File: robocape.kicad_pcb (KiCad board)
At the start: 4 copper layers, 86.4 x 54.6 mm, 110 parts, among them J1 SMA, Q1 2N7002, SW1 SW_PUSH, U1 BEAGLEBONE, U10 MPU-9250, U11 MS5611-01BA, U2 CAT24C256W, U3 BQ32000, U4 XBee_Header, U5 PCA9685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

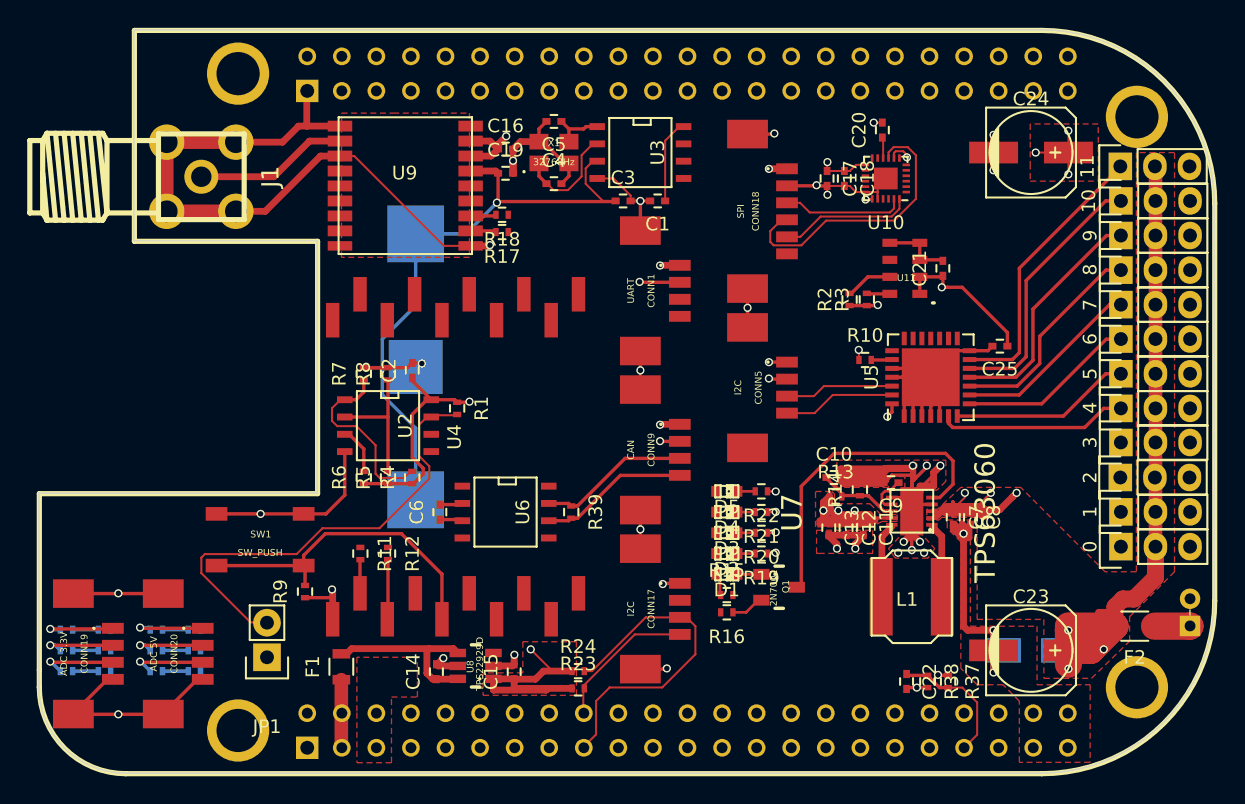
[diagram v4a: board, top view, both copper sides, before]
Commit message: PCB: More tracks
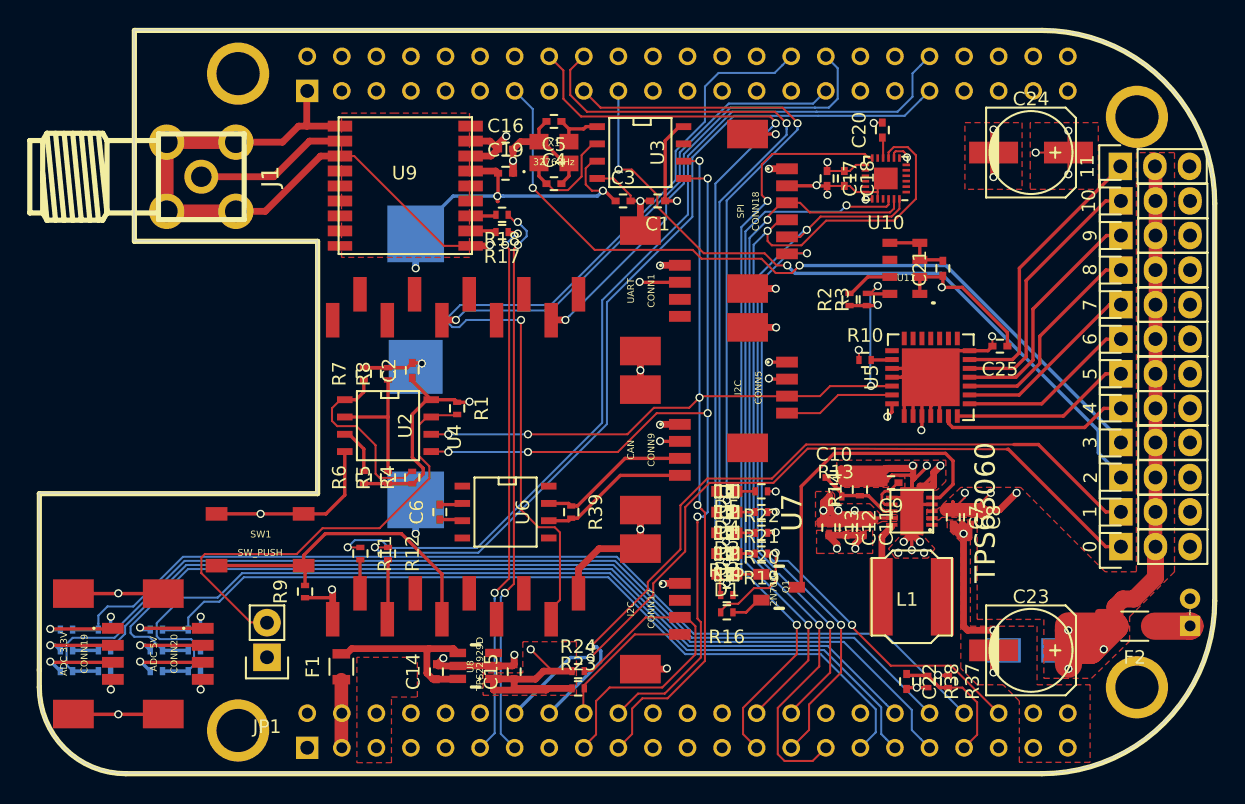
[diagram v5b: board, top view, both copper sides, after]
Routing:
- net /Connectivity/I2C2_SCL: track 9.73 -> 97.3 mm, vias 0 -> 7
- net /Connectivity/ADC_3: track 1.89 -> 74.9 mm
- net /Connectivity/ADC_1: track 1.89 -> 73.1 mm
- net /Connectivity/ADC_2: track 1.89 -> 72.4 mm
- net /Connectivity/ADC_6: track 1.89 -> 70.4 mm
- net /Connectivity/XBEE_TX: track 0.00 -> 67.9 mm, vias 0 -> 1
- net /Connectivity/I2C2_SDA: track 11.7 -> 78.6 mm, vias 0 -> 5
- net /Connectivity/XBEE_DTR: track 0.00 -> 66.3 mm, vias 0 -> 1
- net /Connectivity/ADC_5: track 1.89 -> 67.6 mm
- net /Connectivity/XBEE_RX: track 0.00 -> 63.7 mm, vias 0 -> 1
- net /Connectivity/ADC_4: track 1.89 -> 61.8 mm
- net /Connectivity/PWM_3: track 0.00 -> 59.2 mm, vias 0 -> 2
- net /Connectivity/PWM_0: track 0.00 -> 58.0 mm, vias 0 -> 1
- net /Connectivity/PWM_1: track 0.00 -> 56.4 mm, vias 0 -> 1
- net /Sensors/MPU9250_INT: track 0.00 -> 56.1 mm, vias 0 -> 2
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
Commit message: PCB: More and more tracks
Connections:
- U10 pad 25: (no net) -> GND
- U5 pad 29: (no net) -> GND
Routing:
- net /Connectivity/UART_EXT_TX: track 0.00 -> 41.3 mm, vias 0 -> 2
- net /Connectivity/UART_EXT_RX: track 0.00 -> 37.3 mm, vias 0 -> 2
- net /Connectivity/CAN_TX: track 0.00 -> 35.9 mm, vias 0 -> 1
- net /Connectivity/PWMGEN_OE: track 1.54 -> 34.9 mm, vias 0 -> 2
- net /Connectivity/CAN_RX: track 0.00 -> 28.1 mm, vias 0 -> 1
- net /Power/3.3V_A_EN: track 0.00 -> 19.2 mm, vias 0 -> 1
- net /Connectivity/I2C2_SDA: track 78.6 -> 96.9 mm, vias 5 -> 7
- net +3V3: track 16.9 -> 27.6 mm, vias 2 -> 3
- net GND: track 403.4 -> 393.3 mm, vias 47 -> 51
- net POWER: track 122.9 -> 129.7 mm
- net Net-(L1-Pad1): track 0.06 -> 5.67 mm
- net /Power/PWR_GOOD: track 23.8 -> 28.6 mm
- net +3.3V_A: track 67.7 -> 69.2 mm
- net +5V: track 75.5 -> 74.5 mm
- net /Sensors/MPU9250_MOSI: track 54.0 -> 54.6 mm

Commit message: PCB: Done
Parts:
- added G***: LOGO, _logo:EPFL-LOGO, B.Cu at (145.4, 65.9)
- CONN19: value ADC 3.3V -> ADC3.3V
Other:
- board text added: "Robotics Cape Mk.3 Designed by Salah-Eddine Missri For the Automatic Control Laboratory (LA), EPFL"

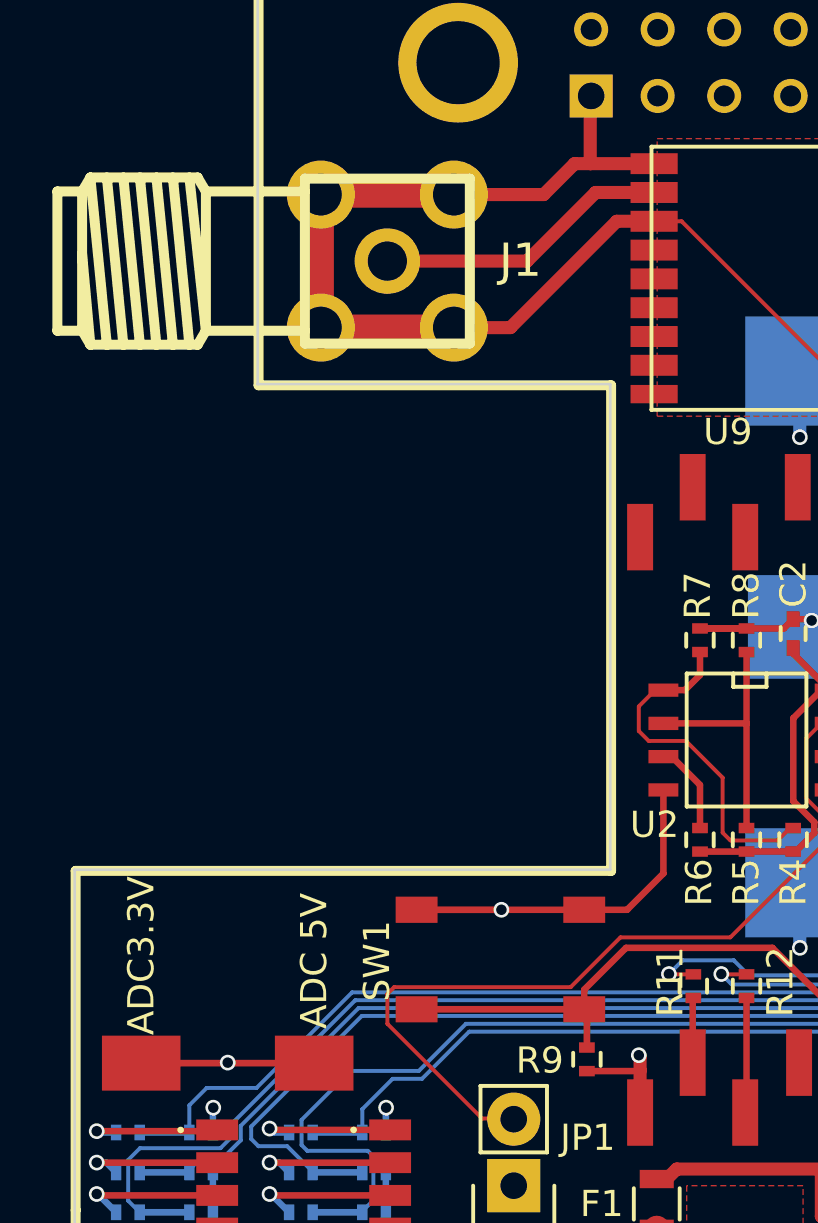
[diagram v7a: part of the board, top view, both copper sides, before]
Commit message: Correct GPS schematic/layout to account for active antenna
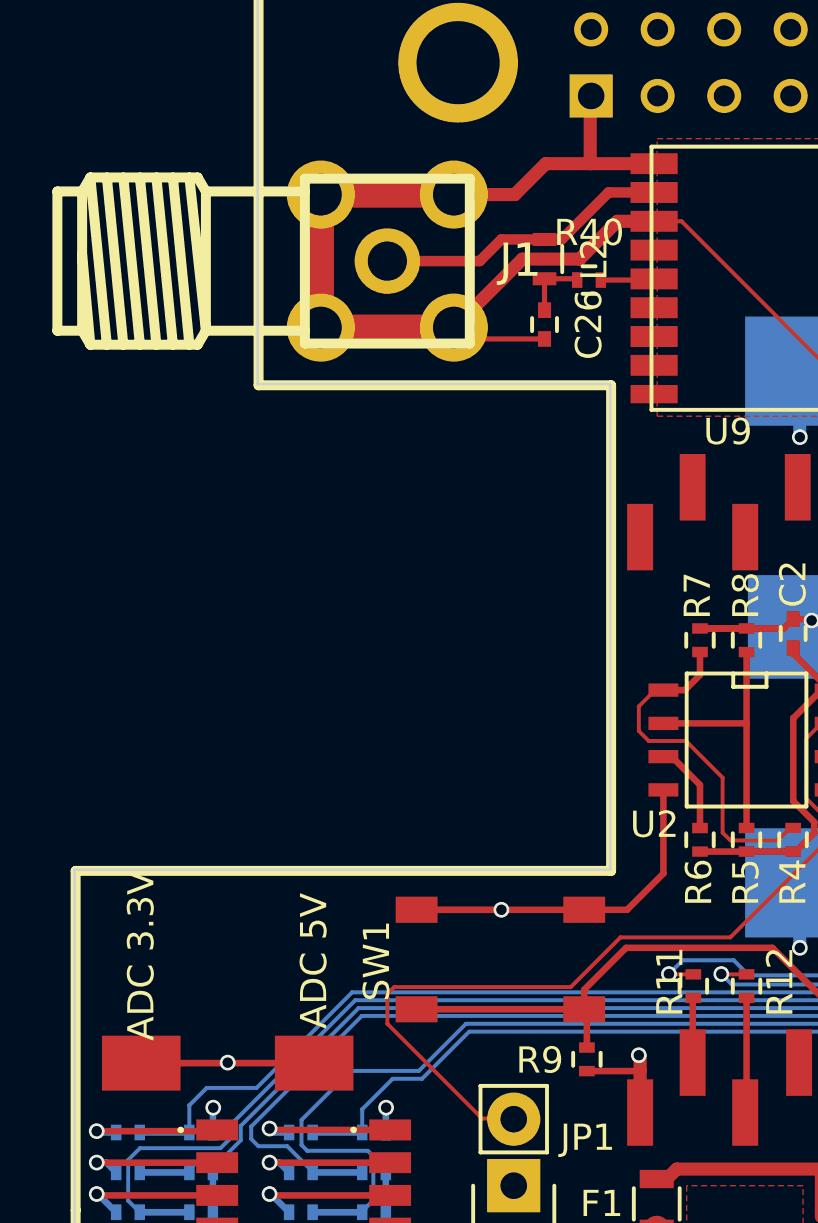
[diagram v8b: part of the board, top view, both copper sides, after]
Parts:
- added C26: C, Capacitors_SMD:C_0402, F.Cu at (91.6, 51.7)
- added L2: L, Resistors_SMD:R_0603, F.Cu at (91.6, 49.2)
- added R40: 10, Resistors_SMD:R_0402, F.Cu at (93.3, 50.0)
- CONN19: value ADC3.3V -> ADC 3.3V
- moved G*** 6.93 mm to (143.0, 72.4), turned to 180 degrees
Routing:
- net GND: track 393.3 -> 396.9 mm
- net Net-(C26-Pad1): track 0.00 -> 2.47 mm
- net Net-(R40-Pad2): track 0.00 -> 2.05 mm
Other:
- board text added: "Robotics Cape Mk.3 Designed by Salah-Eddine Missri Supervised by Andrea Alessandretti Prof. Colin Jones Automatic Control Laboratory (LA), EPFL"
- board text removed: "Robotics Cape Mk.3 Designed by Salah-Eddine Missri For the Automatic Control Laboratory (LA), EPFL"
